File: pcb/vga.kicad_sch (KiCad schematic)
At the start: 18 parts

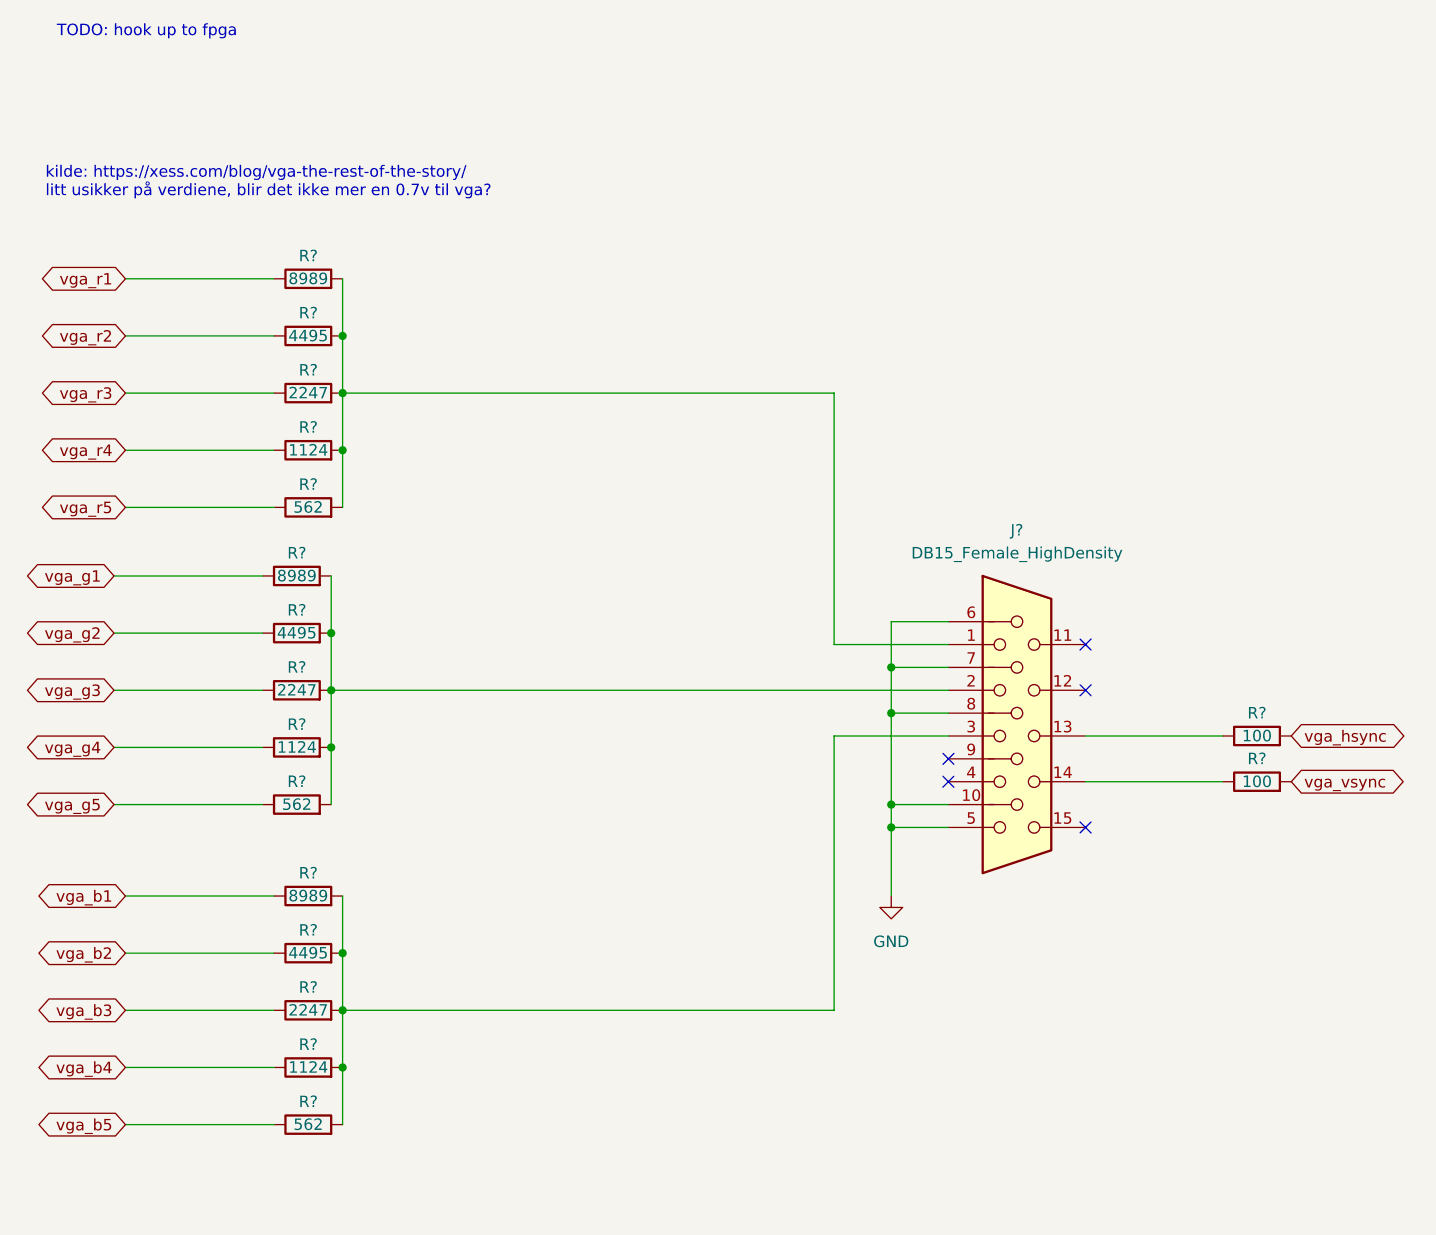
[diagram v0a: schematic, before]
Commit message: connect sram and vga to fpga
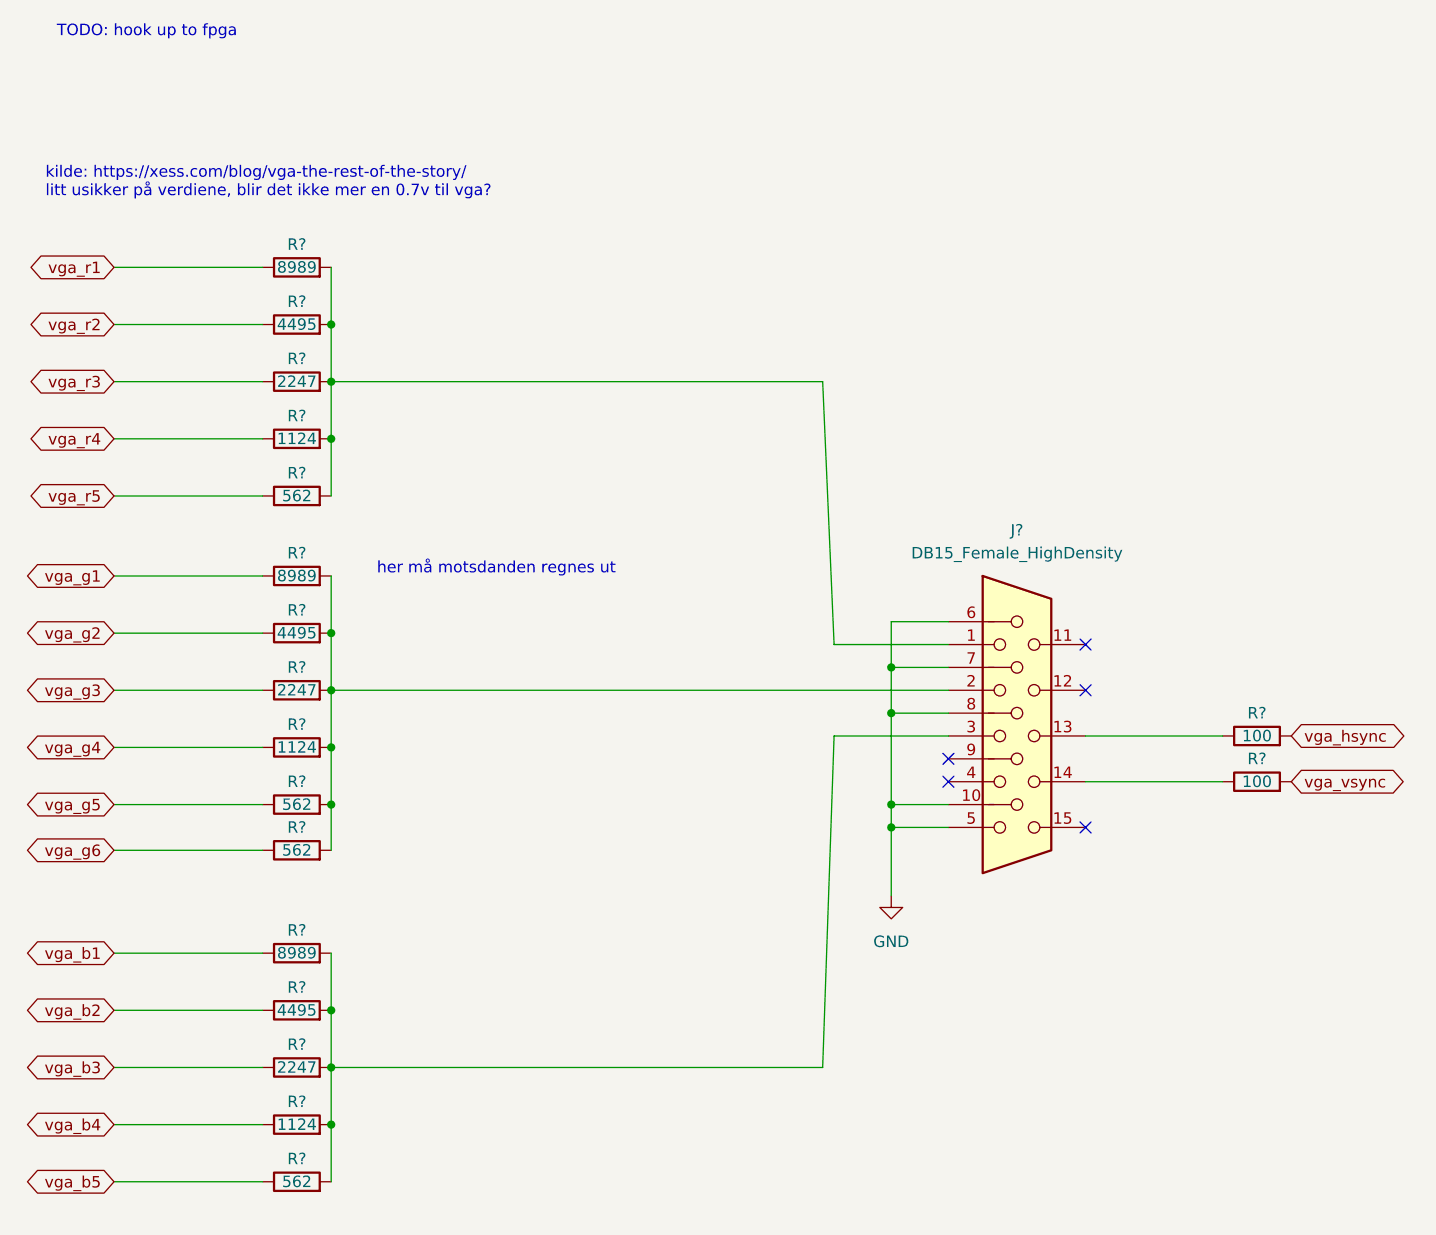
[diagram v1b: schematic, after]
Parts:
- added R?: 562, symbol Device:R
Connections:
- net at J?.2, R?.2, R?.2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: now also R?.2
- new net vga_g6: R?.1
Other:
- note added: "her må motsdanden regnes ut"
- moved on the sheet: R?

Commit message: maybe finished schematic
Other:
- note added: "These are the exact values, we will have to approximate them."
- note removed: "TODO: hook up to fpga"
- note removed: "her må motsdanden regnes ut"
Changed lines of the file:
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@@
     (stroke (width 0) (type default) (color 0 0 0 0))
   )
-  (text "her må motsdanden regnes ut" (at 55.88 77.47 0)
+  (text "These are the exact values, we will have to approximate them."
+    (at 53.975 44.45 0)
     (effects (font (size 1.27 1.27)) (justify left bottom))
   )
-  (text "TODO: hook up to fpga\n" (at 20.32 17.78 0)
-    (effects (font (size 1.27 1.27)) (justify left bottom))
-  )

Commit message: add footprints
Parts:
- R601, R602, R603, R604, R605, R606, R607, R608, R609, R610, R611, R612, R613, R614, R615, R616, R617, R618: renamed from R?; footprint (none) -> Resistor_SMD:R_0805_2012Metric_Pad1.20x1.40mm_HandSolder
- gave numbers to parts that had none: 1
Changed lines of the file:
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@@
   (symbol (lib_id "Connector:DB15_Female_HighDensity") (at 127 95.25 0) (unit 1)
     (in_bom yes) (on_board yes) (fields_autoplaced)
-    (property "Reference" "J?" (id 0) (at 127 72.39 0))
+    (property "Reference" "J601" (id 0) (at 127 72.39 0))
     (property "Value" "DB15_Female_HighDensity" (id 1) (at 127 74.93 0))
     (property "Footprint" "vga:618015330923" (id 2) (at 102.87 85.09 0)
@@
   (symbol (lib_id "Device:R") (at 153.67 100.33 90) (unit 1)
     (in_bom yes) (on_board yes)
-    (property "Reference" "R?" (id 0) (at 153.67 97.79 90))
+    (property "Reference" "R618" (id 0) (at 153.67 97.79 90))
     (property "Value" "100" (id 1) (at 153.67 100.33 90))
-    (property "Footprint" "" (id 2) (at 153.67 102.108 90)
+    (property "Footprint" "Resistor_SMD:R_0805_2012Metric_Pad1.20x1.40mm_HandSolder" (id 2) (at 153.67 102.108 90)
       (effects (font (size 1.27 1.27)) hide)
     )
@@
   (symbol (lib_id "Device:R") (at 46.99 102.87 90) (unit 1)
     (in_bom yes) (on_board yes)
-    (property "Reference" "R?" (id 0) (at 46.99 100.33 90))
+    (property "Reference" "R610" (id 0) (at 46.99 100.33 90))
     (property "Value" "562" (id 1) (at 46.99 102.87 90))
-    (property "Footprint" "" (id 2) (at 46.99 104.648 90)
+    (property "Footprint" "Resistor_SMD:R_0805_2012Metric_Pad1.20x1.40mm_HandSolder" (id 2) (at 46.99 104.648 90)
       (effects (font (size 1.27 1.27)) hide)
     )
@@
   (symbol (lib_id "Device:R") (at 46.99 96.52 90) (unit 1)
     (in_bom yes) (on_board yes)
-    (property "Reference" "R?" (id 0) (at 46.99 93.98 90))
+    (property "Reference" "R609" (id 0) (at 46.99 93.98 90))
     (property "Value" "1124" (id 1) (at 46.99 96.52 90))
-    (property "Footprint" "" (id 2) (at 46.99 98.298 90)
+    (property "Footprint" "Resistor_SMD:R_0805_2012Metric_Pad1.20x1.40mm_HandSolder" (id 2) (at 46.99 98.298 90)
       (effects (font (size 1.27 1.27)) hide)
     )
@@
   (symbol (lib_id "Device:R") (at 46.99 62.23 90) (unit 1)
     (in_bom yes) (on_board yes)
-    (property "Reference" "R?" (id 0) (at 46.99 59.69 90))
+    (property "Reference" "R604" (id 0) (at 46.99 59.69 90))
     (property "Value" "1124" (id 1) (at 46.99 62.23 90))
-    (property "Footprint" "" (id 2) (at 46.99 64.008 90)
+    (property "Footprint" "Resistor_SMD:R_0805_2012Metric_Pad1.20x1.40mm_HandSolder" (id 2) (at 46.99 64.008 90)
       (effects (font (size 1.27 1.27)) hide)
     )
@@
   (symbol (lib_id "power:GND") (at 113.03 113.03 0) (unit 1)
     (in_bom yes) (on_board yes) (fields_autoplaced)
-    (property "Reference" "#PWR?" (id 0) (at 113.03 119.38 0)
+    (property "Reference" "#PWR0601" (id 0) (at 113.03 119.38 0)
       (effects (font (size 1.27 1.27)) hide)
     )
@@
   (symbol (lib_id "Device:R") (at 153.67 95.25 90) (unit 1)
     (in_bom yes) (on_board yes)
-    (property "Reference" "R?" (id 0) (at 153.67 92.71 90))
+    (property "Reference" "R617" (id 0) (at 153.67 92.71 90))
     (property "Value" "100" (id 1) (at 153.67 95.25 90))
-    (property "Footprint" "" (id 2) (at 153.67 97.028 90)
+    (property "Footprint" "Resistor_SMD:R_0805_2012Metric_Pad1.20x1.40mm_HandSolder" (id 2) (at 153.67 97.028 90)
       (effects (font (size 1.27 1.27)) hide)
     )
@@
   (symbol (lib_id "Device:R") (at 46.99 77.47 90) (unit 1)
     (in_bom yes) (on_board yes)
-    (property "Reference" "R?" (id 0) (at 46.99 74.93 90))
+    (property "Reference" "R606" (id 0) (at 46.99 74.93 90))
     (property "Value" "8989" (id 1) (at 46.99 77.47 90))
-    (property "Footprint" "" (id 2) (at 46.99 79.248 90)
+    (property "Footprint" "Resistor_SMD:R_0805_2012Metric_Pad1.20x1.40mm_HandSolder" (id 2) (at 46.99 79.248 90)
       (effects (font (size 1.27 1.27)) hide)
     )
@@
   (symbol (lib_id "Device:R") (at 46.99 138.43 90) (unit 1)
     (in_bom yes) (on_board yes)
-    (property "Reference" "R?" (id 0) (at 46.99 135.89 90))
+    (property "Reference" "R615" (id 0) (at 46.99 135.89 90))
     (property "Value" "1124" (id 1) (at 46.99 138.43 90))
-    (property "Footprint" "" (id 2) (at 46.99 140.208 90)
+    (property "Footprint" "Resistor_SMD:R_0805_2012Metric_Pad1.20x1.40mm_HandSolder" (id 2) (at 46.99 140.208 90)
       (effects (font (size 1.27 1.27)) hide)
     )
@@
   (symbol (lib_id "Device:R") (at 46.99 119.38 90) (unit 1)
     (in_bom yes) (on_board yes)
-    (property "Reference" "R?" (id 0) (at 46.99 116.84 90))
+    (property "Reference" "R612" (id 0) (at 46.99 116.84 90))
     (property "Value" "8989" (id 1) (at 46.99 119.38 90))
-    (property "Footprint" "" (id 2) (at 46.99 121.158 90)
+    (property "Footprint" "Resistor_SMD:R_0805_2012Metric_Pad1.20x1.40mm_HandSolder" (id 2) (at 46.99 121.158 90)
       (effects (font (size 1.27 1.27)) hide)
     )
@@
   (symbol (lib_id "Device:R") (at 46.99 49.53 90) (unit 1)
     (in_bom yes) (on_board yes)
-    (property "Reference" "R?" (id 0) (at 46.99 46.99 90))
+    (property "Reference" "R602" (id 0) (at 46.99 46.99 90))
     (property "Value" "4495" (id 1) (at 46.99 49.53 90))
-    (property "Footprint" "" (id 2) (at 46.99 51.308 90)
+    (property "Footprint" "Resistor_SMD:R_0805_2012Metric_Pad1.20x1.40mm_HandSolder" (id 2) (at 46.99 51.308 90)
       (effects (font (size 1.27 1.27)) hide)
     )
@@
   (symbol (lib_id "Device:R") (at 46.99 83.82 90) (unit 1)
     (in_bom yes) (on_board yes)
-    (property "Reference" "R?" (id 0) (at 46.99 81.28 90))
+    (property "Reference" "R607" (id 0) (at 46.99 81.28 90))
     (property "Value" "4495" (id 1) (at 46.99 83.82 90))
-    (property "Footprint" "" (id 2) (at 46.99 85.598 90)
+    (property "Footprint" "Resistor_SMD:R_0805_2012Metric_Pad1.20x1.40mm_HandSolder" (id 2) (at 46.99 85.598 90)
       (effects (font (size 1.27 1.27)) hide)
     )
@@
   (symbol (lib_id "Device:R") (at 46.99 90.17 90) (unit 1)
     (in_bom yes) (on_board yes)
-    (property "Reference" "R?" (id 0) (at 46.99 87.63 90))
+    (property "Reference" "R608" (id 0) (at 46.99 87.63 90))
     (property "Value" "2247" (id 1) (at 46.99 90.17 90))
-    (property "Footprint" "" (id 2) (at 46.99 91.948 90)
+    (property "Footprint" "Resistor_SMD:R_0805_2012Metric_Pad1.20x1.40mm_HandSolder" (id 2) (at 46.99 91.948 90)
       (effects (font (size 1.27 1.27)) hide)
     )
@@
   (symbol (lib_id "Device:R") (at 46.99 107.95 90) (unit 1)
     (in_bom yes) (on_board yes)
-    (property "Reference" "R?" (id 0) (at 46.99 105.41 90))
+    (property "Reference" "R611" (id 0) (at 46.99 105.41 90))
     (property "Value" "562" (id 1) (at 46.99 107.95 90))
-    (property "Footprint" "" (id 2) (at 46.99 109.728 90)
+    (property "Footprint" "Resistor_SMD:R_0805_2012Metric_Pad1.20x1.40mm_HandSolder" (id 2) (at 46.99 109.728 90)
       (effects (font (size 1.27 1.27)) hide)
     )
@@
   (symbol (lib_id "Device:R") (at 46.99 132.08 90) (unit 1)
     (in_bom yes) (on_board yes)
-    (property "Reference" "R?" (id 0) (at 46.99 129.54 90))
+    (property "Reference" "R614" (id 0) (at 46.99 129.54 90))
     (property "Value" "2247" (id 1) (at 46.99 132.08 90))
-    (property "Footprint" "" (id 2) (at 46.99 133.858 90)
+    (property "Footprint" "Resistor_SMD:R_0805_2012Metric_Pad1.20x1.40mm_HandSolder" (id 2) (at 46.99 133.858 90)
       (effects (font (size 1.27 1.27)) hide)
     )
@@
   (symbol (lib_id "Device:R") (at 46.99 43.18 90) (unit 1)
     (in_bom yes) (on_board yes)
-    (property "Reference" "R?" (id 0) (at 46.99 40.64 90))
+    (property "Reference" "R601" (id 0) (at 46.99 40.64 90))
     (property "Value" "8989" (id 1) (at 46.99 43.18 90))
-    (property "Footprint" "" (id 2) (at 46.99 44.958 90)
+    (property "Footprint" "Resistor_SMD:R_0805_2012Metric_Pad1.20x1.40mm_HandSolder" (id 2) (at 46.99 44.958 90)
       (effects (font (size 1.27 1.27)) hide)
     )
@@
   (symbol (lib_id "Device:R") (at 46.99 144.78 90) (unit 1)
     (in_bom yes) (on_board yes)
-    (property "Reference" "R?" (id 0) (at 46.99 142.24 90))
+    (property "Reference" "R616" (id 0) (at 46.99 142.24 90))
     (property "Value" "562" (id 1) (at 46.99 144.78 90))
-    (property "Footprint" "" (id 2) (at 46.99 146.558 90)
+    (property "Footprint" "Resistor_SMD:R_0805_2012Metric_Pad1.20x1.40mm_HandSolder" (id 2) (at 46.99 146.558 90)
       (effects (font (size 1.27 1.27)) hide)
     )
@@
   (symbol (lib_id "Device:R") (at 46.99 68.58 90) (unit 1)
     (in_bom yes) (on_board yes)
-    (property "Reference" "R?" (id 0) (at 46.99 66.04 90))
+    (property "Reference" "R605" (id 0) (at 46.99 66.04 90))
     (property "Value" "562" (id 1) (at 46.99 68.58 90))
-    (property "Footprint" "" (id 2) (at 46.99 70.358 90)
+    (property "Footprint" "Resistor_SMD:R_0805_2012Metric_Pad1.20x1.40mm_HandSolder" (id 2) (at 46.99 70.358 90)
       (effects (font (size 1.27 1.27)) hide)
     )
@@
   (symbol (lib_id "Device:R") (at 46.99 125.73 90) (unit 1)
     (in_bom yes) (on_board yes)
-    (property "Reference" "R?" (id 0) (at 46.99 123.19 90))
+    (property "Reference" "R613" (id 0) (at 46.99 123.19 90))
     (property "Value" "4495" (id 1) (at 46.99 125.73 90))
-    (property "Footprint" "" (id 2) (at 46.99 127.508 90)
+    (property "Footprint" "Resistor_SMD:R_0805_2012Metric_Pad1.20x1.40mm_HandSolder" (id 2) (at 46.99 127.508 90)
       (effects (font (size 1.27 1.27)) hide)
     )
@@
   (symbol (lib_id "Device:R") (at 46.99 55.88 90) (unit 1)
     (in_bom yes) (on_board yes)
-    (property "Reference" "R?" (id 0) (at 46.99 53.34 90))
+    (property "Reference" "R603" (id 0) (at 46.99 53.34 90))
     (property "Value" "2247" (id 1) (at 46.99 55.88 90))
-    (property "Footprint" "" (id 2) (at 46.99 57.658 90)
-      (effects (font (size 1.27 1.27)) hide)
-    )
+    (property "Footprint" "Resistor_SMD:R_0805_2012Metric_Pad1.20x1.40mm_HandSolder" (id 2) (at 46.99 57.658 90)
+      (effects (font (size 1.27 1.27)) hide)
+    )

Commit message: fix vga resistors
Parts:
- removed R606, R612: 8989, Resistor_SMD:R_0805_2012Metric_Pad1.20x1.40mm_HandSolder, symbol Device:R
- removed R607, R613: 4495, Resistor_SMD:R_0805_2012Metric_Pad1.20x1.40mm_HandSolder, symbol Device:R
- removed R608, R614: 2247, Resistor_SMD:R_0805_2012Metric_Pad1.20x1.40mm_HandSolder, symbol Device:R
- removed R609, R615: 1124, Resistor_SMD:R_0805_2012Metric_Pad1.20x1.40mm_HandSolder, symbol Device:R
- removed R610, R611, R616: 562, Resistor_SMD:R_0805_2012Metric_Pad1.20x1.40mm_HandSolder, symbol Device:R
- added R? (x2): 1300, Resistor_SMD:R_0603_1608Metric_Pad0.98x0.95mm_HandSolder, symbol Device:R
- added R? (x2): 4420, Resistor_SMD:R_0603_1608Metric_Pad0.98x0.95mm_HandSolder, symbol Device:R
- added R? (x2): 550, Resistor_SMD:R_0603_1608Metric_Pad0.98x0.95mm_HandSolder, symbol Device:R
- added R?: 17400, Resistor_SMD:R_0603_1608Metric_Pad0.98x0.95mm_HandSolder, symbol Device:R
- added R? (x2): 8760, Resistor_SMD:R_0603_1608Metric_Pad0.98x0.95mm_HandSolder, symbol Device:R
- added R? (x2): 2200, Resistor_SMD:R_0603_1608Metric_Pad0.98x0.95mm_HandSolder, symbol Device:R
- R601: value 8989 -> 8760; footprint Resistor_SMD:R_0805_2012Metric_Pad1.20x1.40mm_HandSolder -> Resistor_SMD:R_0603_1608Metric_Pad0.98x0.95mm_HandSolder
- R602: value 4495 -> 4420; footprint Resistor_SMD:R_0805_2012Metric_Pad1.20x1.40mm_HandSolder -> Resistor_SMD:R_0603_1608Metric_Pad0.98x0.95mm_HandSolder
- R603: value 2247 -> 2200; footprint Resistor_SMD:R_0805_2012Metric_Pad1.20x1.40mm_HandSolder -> Resistor_SMD:R_0603_1608Metric_Pad0.98x0.95mm_HandSolder
- R604: value 1124 -> 1300; footprint Resistor_SMD:R_0805_2012Metric_Pad1.20x1.40mm_HandSolder -> Resistor_SMD:R_0603_1608Metric_Pad0.98x0.95mm_HandSolder
- R605: value 562 -> 550; footprint Resistor_SMD:R_0805_2012Metric_Pad1.20x1.40mm_HandSolder -> Resistor_SMD:R_0603_1608Metric_Pad0.98x0.95mm_HandSolder
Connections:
- net vga_b1: now also R?.1
- net vga_b2: now also R?.1
- net vga_b3: now also R?.1
- net vga_b4: now also R?.1
- net vga_b5: now also R?.1
- net vga_g1: now also R?.1
- net vga_g2: now also R?.1
- net vga_g3: now also R?.1
- net vga_g4: now also R?.1
- net vga_g5: now also R?.1
- net vga_g6: now also R?.1
- net at J601.2: now also R?.2, R?.2, R?.2, R?.2, R?.2, R?.2
- net at J601.3: now also R?.2, R?.2, R?.2, R?.2, R?.2

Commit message: fix joystick
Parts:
- removed R? (x2): 1300, Resistor_SMD:R_0603_1608Metric_Pad0.98x0.95mm_HandSolder, symbol Device:R
- removed R? (x2): 4420, Resistor_SMD:R_0603_1608Metric_Pad0.98x0.95mm_HandSolder, symbol Device:R
- removed R? (x2): 550, Resistor_SMD:R_0603_1608Metric_Pad0.98x0.95mm_HandSolder, symbol Device:R
- removed R?: 17400, Resistor_SMD:R_0603_1608Metric_Pad0.98x0.95mm_HandSolder, symbol Device:R
- removed R? (x2): 8760, Resistor_SMD:R_0603_1608Metric_Pad0.98x0.95mm_HandSolder, symbol Device:R
- removed R? (x2): 2200, Resistor_SMD:R_0603_1608Metric_Pad0.98x0.95mm_HandSolder, symbol Device:R
- added R606, R612: 8989, Resistor_SMD:R_0805_2012Metric_Pad1.20x1.40mm_HandSolder, symbol Device:R
- added R607, R613: 4495, Resistor_SMD:R_0805_2012Metric_Pad1.20x1.40mm_HandSolder, symbol Device:R
- added R608, R614: 2247, Resistor_SMD:R_0805_2012Metric_Pad1.20x1.40mm_HandSolder, symbol Device:R
- added R609, R615: 1124, Resistor_SMD:R_0805_2012Metric_Pad1.20x1.40mm_HandSolder, symbol Device:R
- added R610, R611, R616: 562, Resistor_SMD:R_0805_2012Metric_Pad1.20x1.40mm_HandSolder, symbol Device:R
- R601: value 8760 -> 8989; footprint Resistor_SMD:R_0603_1608Metric_Pad0.98x0.95mm_HandSolder -> Resistor_SMD:R_0805_2012Metric_Pad1.20x1.40mm_HandSolder
- R602: value 4420 -> 4495; footprint Resistor_SMD:R_0603_1608Metric_Pad0.98x0.95mm_HandSolder -> Resistor_SMD:R_0805_2012Metric_Pad1.20x1.40mm_HandSolder
- R603: value 2200 -> 2247; footprint Resistor_SMD:R_0603_1608Metric_Pad0.98x0.95mm_HandSolder -> Resistor_SMD:R_0805_2012Metric_Pad1.20x1.40mm_HandSolder
- R604: value 1300 -> 1124; footprint Resistor_SMD:R_0603_1608Metric_Pad0.98x0.95mm_HandSolder -> Resistor_SMD:R_0805_2012Metric_Pad1.20x1.40mm_HandSolder
- R605: value 550 -> 562; footprint Resistor_SMD:R_0603_1608Metric_Pad0.98x0.95mm_HandSolder -> Resistor_SMD:R_0805_2012Metric_Pad1.20x1.40mm_HandSolder
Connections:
- net vga_b1: now also R612.1
- net vga_b2: now also R613.1
- net vga_b3: now also R614.1
- net vga_b4: now also R615.1
- net vga_b5: now also R616.1
- net vga_g1: now also R606.1
- net vga_g2: now also R607.1
- net vga_g3: now also R608.1
- net vga_g4: now also R609.1
- net vga_g5: now also R610.1
- net vga_g6: now also R611.1
- net at J601.3: now also R612.2, R613.2, R614.2, R615.2, R616.2
- net at J601.2: now also R606.2, R607.2, R608.2, R609.2, R610.2, R611.2
